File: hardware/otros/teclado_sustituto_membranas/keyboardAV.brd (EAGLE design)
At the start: 260 x 110 mm, 98 parts, among them IC1 74HC32, IC2 74LS244DW

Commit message: 
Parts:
- moved D3 63.8 mm to (10.5, 80.6), turned to 180 degrees
- moved D2 51.6 mm to (19.1, 91.8), turned to 270 degrees
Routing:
- net A9: track 0.00 -> 117.7 mm
- net A10: track 0.00 -> 96.6 mm
- net A11: track 0.00 -> 82.0 mm
- net N$49: track 0.00 -> 63.4 mm
- net A14: track 0.00 -> 48.2 mm
- net N$60: track 0.00 -> 45.6 mm
- net A13: track 0.00 -> 34.4 mm
- net A8: track 0.00 -> 31.1 mm
- net N$53: track 0.00 -> 29.9 mm
- net N$12: track 0.00 -> 25.6 mm
- net N$6: track 0.00 -> 25.5 mm
- net N$20: track 0.00 -> 25.4 mm
- net N$45: track 0.00 -> 25.3 mm
- net N$23: track 0.00 -> 25.2 mm
- net N$13: track 0.00 -> 25.1 mm
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
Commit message: 
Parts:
- moved D1 170.5 mm to (234.3, 76.2)
- moved D4 135.4 mm to (214.9, 86.4), turned to 270 degrees
- moved D5 133.6 mm to (205.4, 20.3)
- moved D32 108.8 mm to (167.0, 71.8), turned to 90 degrees
- moved D21 102.3 mm to (166.7, 38.1), turned to 270 degrees
- moved D29 81.4 mm to (187.3, 71.8), turned to 90 degrees
- moved D8 77.9 mm to (181.9, 71.8), turned to 90 degrees
- moved D16 77.8 mm to (169.5, 71.8), turned to 90 degrees
- moved D26 76.8 mm to (164.1, 71.8), turned to 90 degrees
- moved D18 75.0 mm to (179.4, 71.8), turned to 90 degrees
- moved D7 74.4 mm to (172.1, 71.8), turned to 90 degrees
- moved D10 68.8 mm to (184.8, 71.8), turned to 90 degrees
- moved IC1 65.5 mm to (146.1, 45.7), turned to 270 degrees
- moved D9 62.8 mm to (81.9, 24.1), turned to 90 degrees
- moved D6 56.0 mm to (110.2, 26.7)
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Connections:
- removed net N$52: ENTER.2, SPACE.1
- removed net N$8: A.2, CAPS.1, CAPS1.1
- new net N$91: A.2, CAPS.2, CAPS1.1, SPACE.2
- net N$19: now also V.1; no longer V.2
- net N$28: now also V.2; no longer V.1
- net N$54: now also BREAK.2
- net N$9: now also CAPS.1, ENTER.2; no longer BREAK.2, CAPS.2, SPACE.2
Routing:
- net GND: track 0.00 -> 428.3 mm
- net N$16: track 0.00 -> 316.5 mm
- net N$69: track 0.00 -> 254.8 mm
- net N$91: track 0.00 -> 229.7 mm
- net A12: track 11.8 -> 222.6 mm
- net N$60: track 45.6 -> 250.3 mm, vias 0 -> 1
- net A8: track 31.1 -> 146.1 mm, vias 0 -> 1
- net N$17: track 0.00 -> 100.3 mm, vias 0 -> 1
- net N$82: track 0.00 -> 71.5 mm, vias 0 -> 1
- net D4: track 0.00 -> 65.2 mm
- net D0: track 0.00 -> 62.9 mm
- net N$18: track 0.00 -> 60.7 mm, vias 0 -> 1
- net N$88: track 0.00 -> 58.4 mm
- net D2: track 0.00 -> 57.0 mm, vias 0 -> 1
- net D3: track 0.00 -> 49.0 mm
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
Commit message: 
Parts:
- added D34: (no value), diode:SOD323-R
- moved D11 33.0 mm to (56.2, 26.7), turned to 90 degrees
- moved D22 32.6 mm to (47.6, 17.5)
- moved D12 32.3 mm to (59.4, 27.9), turned to 90 degrees
- moved D31 15.6 mm to (69.8, 35.9)
- moved D33 14.0 mm to (77.5, 35.9)
- moved D6 13.0 mm to (97.2, 26.7)
- moved R2 3.49 mm to (93.7, 24.1)
- moved D3 2.01 mm to (20.3, 93.3)
- moved D2 0.63 mm to (8.26, 94.6)
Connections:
- removed net N$69: SPACE.4, SYMB.3, SYMB1.3
- removed net N$76: COMMA.4, PERIOD.3
- removed net N$78: COMMA.2, D11.C
- removed net N$82: D6.C, PERIOD.1, R2.2
- net A15: now also PERIOD.3, SPACE.4, SYMB.3, SYMB1.3; no longer SPACE.3
- net A8: now also D34.C
- net N$73: now also D34.A
- net N$79: now also D6.C, PERIOD.1, R2.2; no longer PERIOD.2
- net N$83: now also COMMA.2, D11.C; no longer COMMA.1
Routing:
- net A15: track 0.00 -> 428.2 mm, vias 0 -> 1
- net N$69: track 254.8 -> 0.00 mm
- net N$82: track 71.5 -> 0.00 mm, vias 1 -> 0
- net N$83: track 7.84 -> 69.4 mm, vias 0 -> 1
- net N$79: track 0.00 -> 55.1 mm, vias 0 -> 1
- net A8: track 146.1 -> 159.8 mm
- net N$4: track 0.00 -> 7.52 mm, vias 0 -> 1
- net N$70: track 72.9 -> 78.1 mm, vias 0 -> 1
- net N$60: track 250.3 -> 246.1 mm
- net N$3: track 0.00 -> 3.82 mm, vias 0 -> 1
- net VCC: track 8.25 -> 4.76 mm

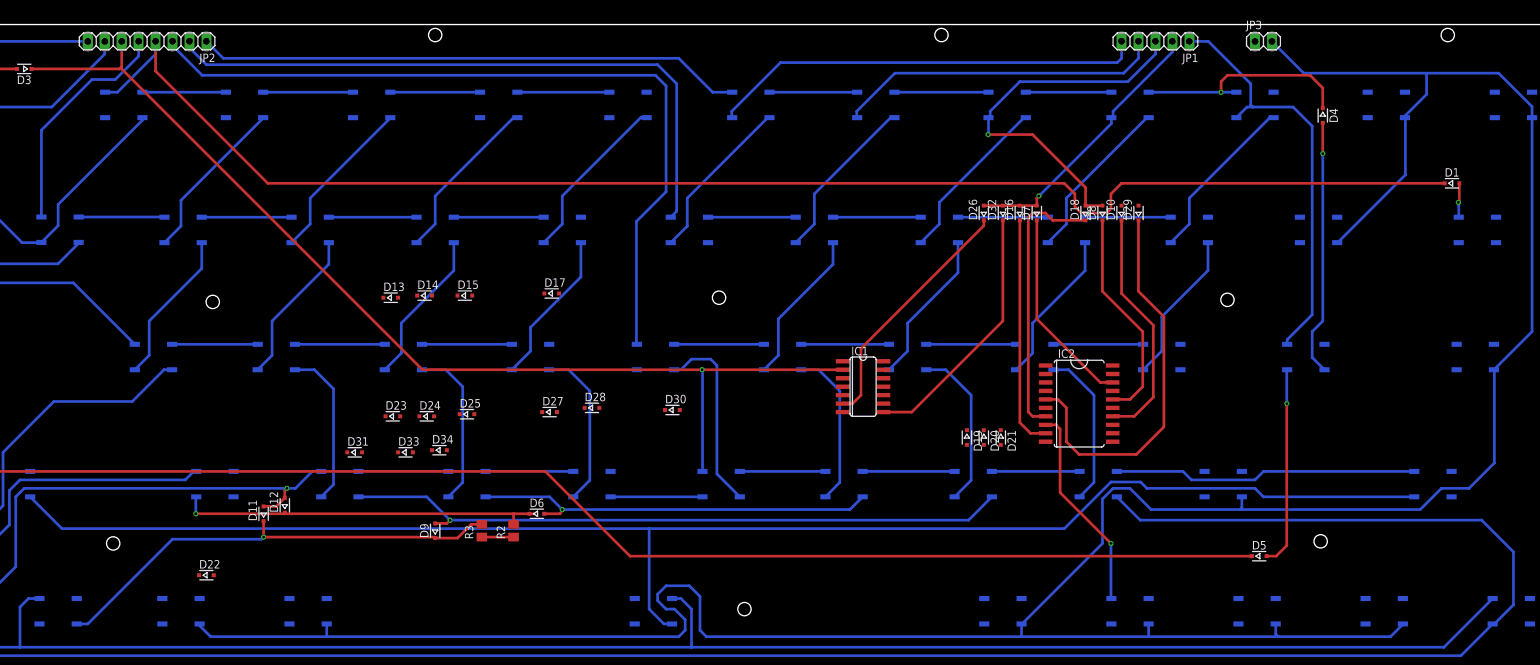
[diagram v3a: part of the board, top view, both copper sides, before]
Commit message: 
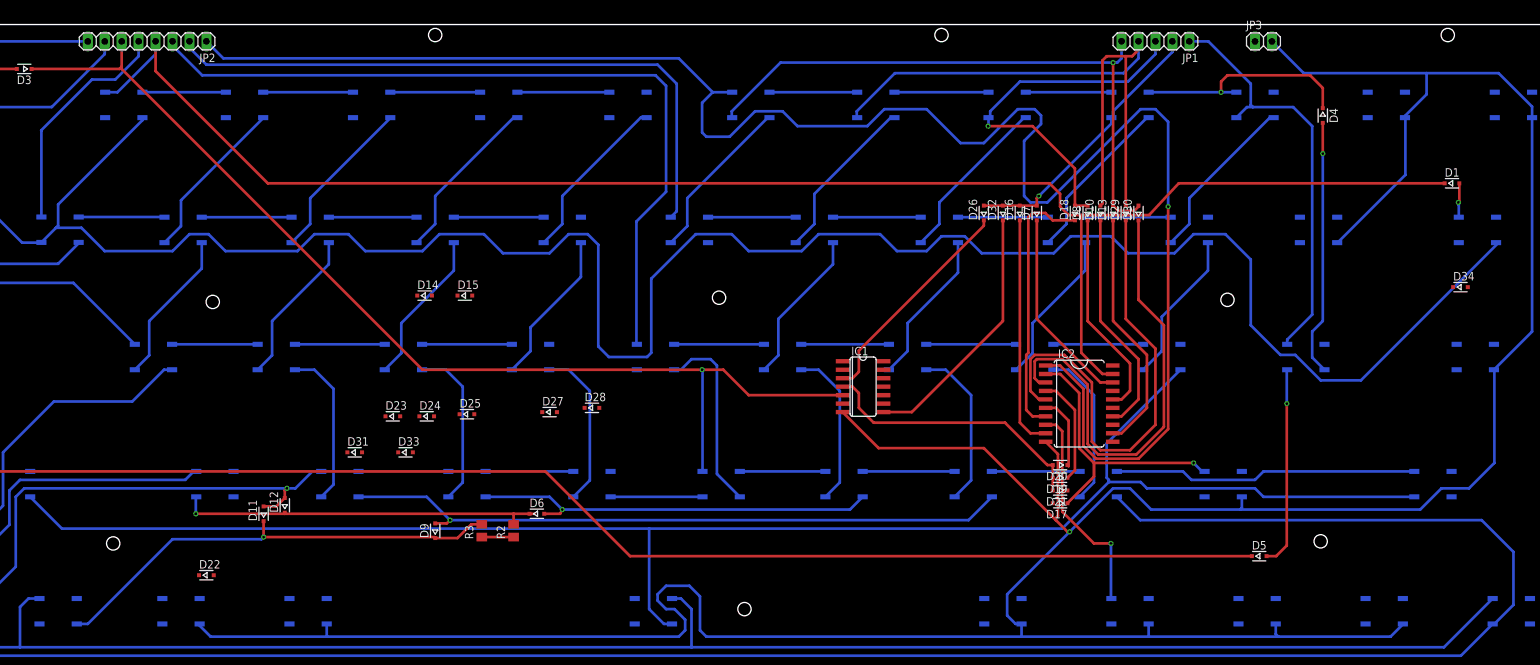
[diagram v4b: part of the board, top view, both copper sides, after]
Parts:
- moved D34 155.0 mm to (235.6, 60.6)
- moved D13 109.0 mm to (183.5, 71.8), turned to 90 degrees
- moved D17 82.4 mm to (175.6, 28.3), turned to 180 degrees
- moved D30 75.8 mm to (187.3, 71.8), turned to 90 degrees
- moved D19 15.2 mm to (175.6, 32.1), turned to 180 degrees
- moved D20 12.2 mm to (175.6, 34.0), turned to 180 degrees
- moved D21 11.9 mm to (175.6, 30.2), turned to 180 degrees
- moved D10 3.17 mm to (181.6, 71.8)
- moved D8 2.22 mm to (179.7, 71.8)
- moved D29 1.91 mm to (185.4, 71.8)
- moved D18 1.59 mm to (177.8, 71.8)
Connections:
- net A15: now also IC1.2; no longer IC1.5
- net A8: now also IC1.5; no longer IC1.2
- net N$84: now also IC1.6; no longer IC1.3
- net N$86: now also IC1.3; no longer IC1.6
- net N$87: now also IC1.1; no longer IC1.4
- net N$90: now also IC1.4; no longer IC1.1
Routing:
- net N$54: track 49.0 -> 337.2 mm
- net A11: track 82.0 -> 266.6 mm, vias 0 -> 1
- net N$89: track 0.00 -> 69.3 mm
- net GND: track 428.3 -> 484.7 mm, vias 0 -> 1
- net D3: track 49.0 -> 100.6 mm
- net CAPSLOCK: track 0.00 -> 42.4 mm, vias 0 -> 1
- net N$90: track 0.00 -> 41.5 mm
- net N$80: track 0.00 -> 36.9 mm
- net D4: track 65.2 -> 91.2 mm, vias 0 -> 1
- net A12: track 222.6 -> 248.3 mm
- net N$91: track 229.7 -> 251.2 mm
- net TRUEV: track 0.00 -> 16.2 mm
- net N$88: track 58.4 -> 71.8 mm
- net INVV: track 0.00 -> 11.3 mm
- net N$86: track 37.1 -> 33.3 mm
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
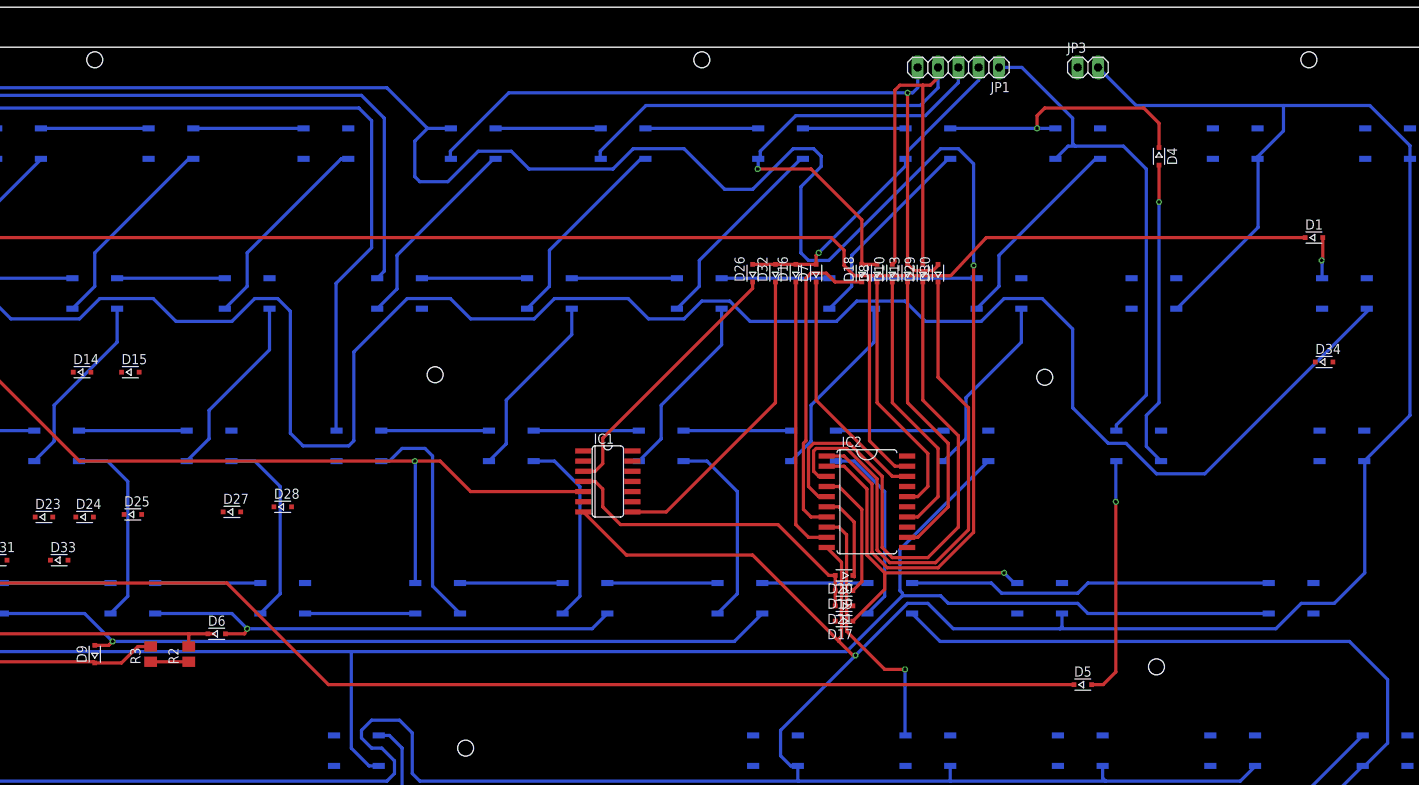
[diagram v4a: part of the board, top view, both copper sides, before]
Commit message: 
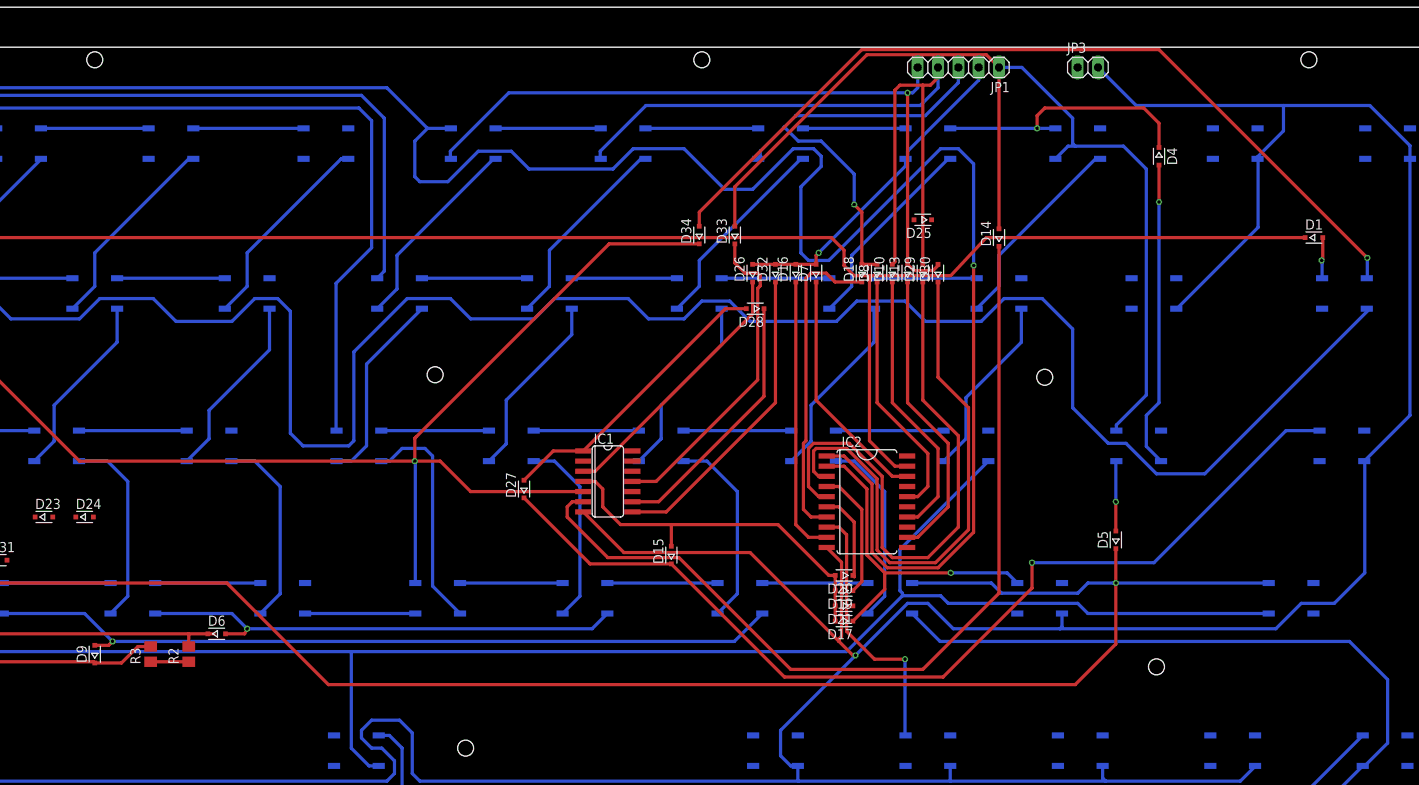
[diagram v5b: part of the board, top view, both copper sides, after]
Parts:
- moved D14 115.8 mm to (194.9, 76.2), turned to 90 degrees
- moved D25 105.4 mm to (185.4, 78.4), turned to 180 degrees
- moved D33 93.7 mm to (161.9, 76.5), turned to 90 degrees
- moved D34 79.7 mm to (157.5, 76.5), turned to 90 degrees
- moved D15 71.4 mm to (154.0, 36.5), turned to 90 degrees
- moved D28 64.0 mm to (164.5, 67.3), turned to 180 degrees
- moved D27 36.6 mm to (135.6, 44.8), turned to 90 degrees
- moved D5 18.6 mm to (209.6, 38.4), turned to 90 degrees
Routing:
- net EXTEND: track 0.00 -> 123.3 mm, vias 0 -> 1
- net N$84: track 0.00 -> 112.7 mm
- net N$73: track 0.00 -> 107.0 mm, vias 0 -> 1
- net D0: track 62.9 -> 128.5 mm
- net A8: track 161.3 -> 209.8 mm
- net N$114: track 0.00 -> 40.3 mm
- net N$87: track 0.00 -> 36.7 mm
- net SEMICOLON: track 0.00 -> 32.9 mm
- net N$27: track 0.00 -> 24.5 mm
- net N$2: track 30.1 -> 8.77 mm
- net N$60: track 246.1 -> 265.3 mm, vias 1 -> 2
- net N$90: track 41.5 -> 46.1 mm
- net LEFT: track 33.3 -> 34.0 mm

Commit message: 
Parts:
- moved D23 112.4 mm to (188.0, 44.8)
- moved D24 107.3 mm to (188.0, 41.9)
- moved D31 85.4 mm to (153.0, 55.2), turned to 90 degrees
- moved D25 39.1 mm to (188.0, 39.4), turned to 0 degrees
- moved D4 0.32 mm to (214.6, 86.4)
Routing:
- net INVV: track 11.3 -> 166.0 mm, vias 0 -> 1
- net TRUEV: track 16.2 -> 137.4 mm, vias 0 -> 1
- net GRAPHICS: track 0.00 -> 51.8 mm, vias 0 -> 3
- net RIGHT: track 0.00 -> 40.9 mm, vias 0 -> 1
- net N$90: track 46.1 -> 74.5 mm, vias 0 -> 2
- net N$91: track 251.2 -> 265.1 mm
- net QUOTES: track 0.00 -> 10.1 mm
- net N$15: track 23.8 -> 29.6 mm
- net UP: track 0.00 -> 4.32 mm
- net N$87: track 36.7 -> 39.0 mm
- net N$86: track 33.3 -> 35.4 mm
- net N$88: track 71.8 -> 72.9 mm
- net GND: track 484.7 -> 485.8 mm
- net A11: track 266.6 -> 267.2 mm
- net N$89: track 69.3 -> 69.9 mm

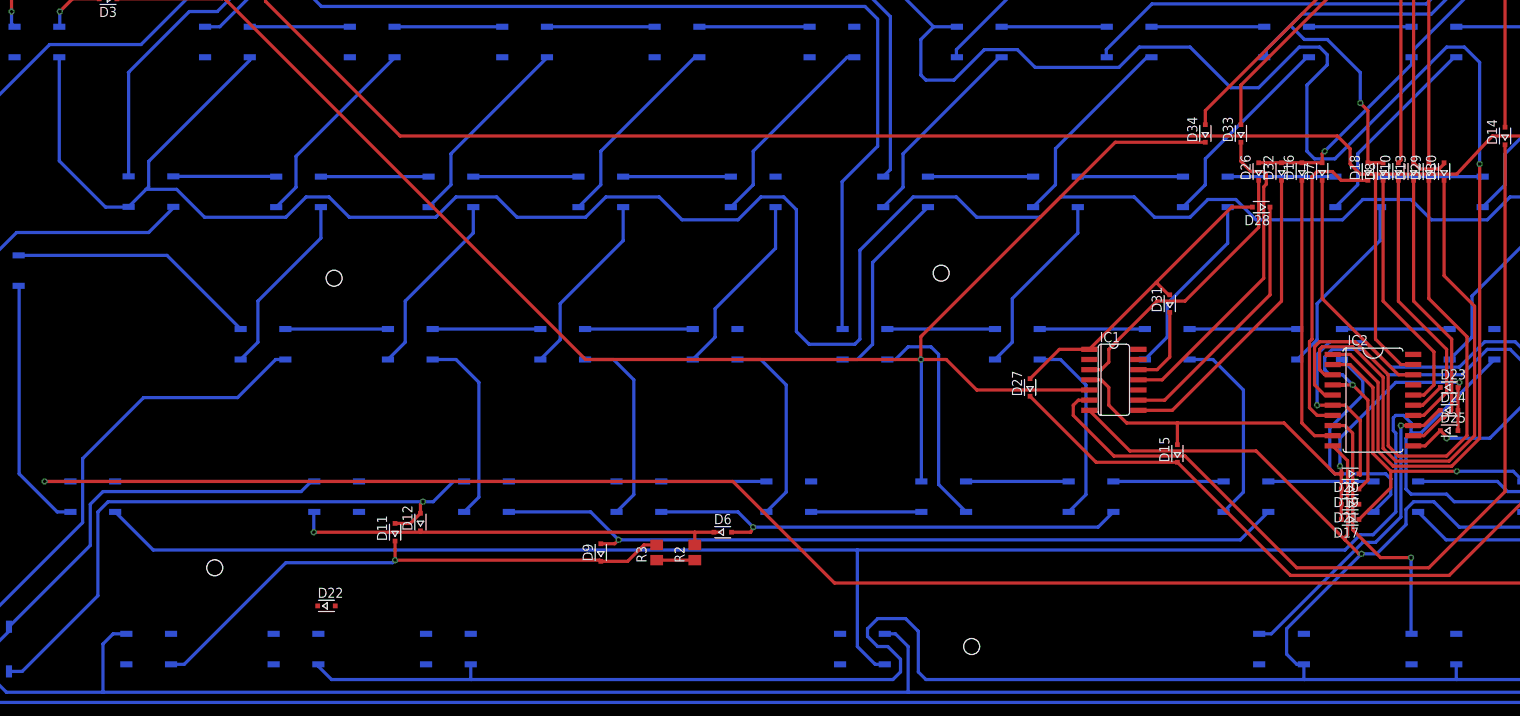
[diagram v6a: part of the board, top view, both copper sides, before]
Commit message: 
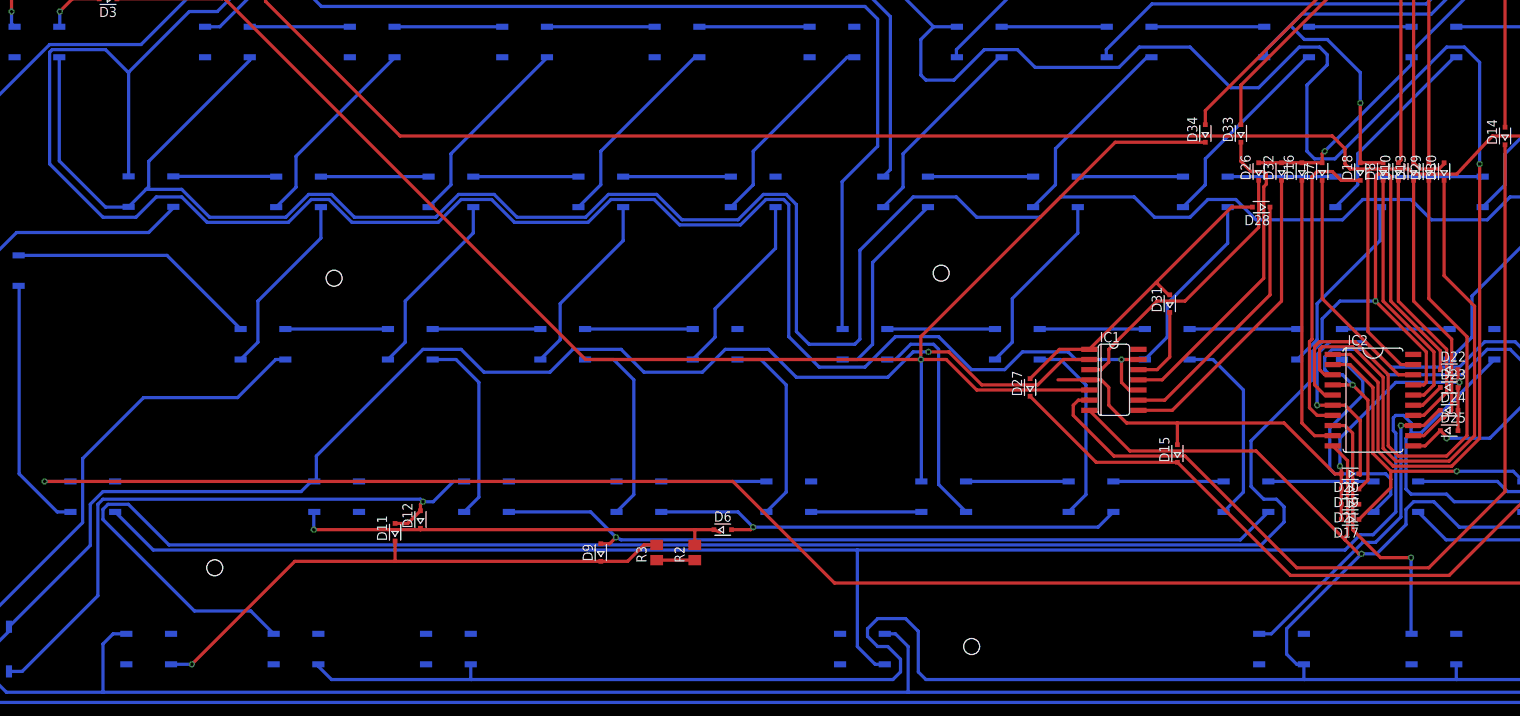
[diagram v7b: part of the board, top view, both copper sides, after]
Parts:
- moved D22 143.4 mm to (188.0, 47.0)
- moved D18 0.95 mm to (176.8, 71.8)
- moved D12 0.32 mm to (59.4, 28.3)
- moved D6 0.32 mm to (97.2, 27.0)
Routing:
- net DOWN: track 0.00 -> 278.0 mm, vias 0 -> 1
- net A13: track 34.4 -> 237.7 mm, vias 0 -> 1
- net A15: track 428.2 -> 544.1 mm, vias 1 -> 2
- net N$90: track 74.5 -> 80.1 mm
- net N$54: track 337.2 -> 338.6 mm
- net A12: track 248.3 -> 249.3 mm
- net N$85: track 40.0 -> 39.1 mm
- net N$70: track 78.1 -> 78.8 mm
- net N$28: track 28.6 -> 29.2 mm
- net D2: track 56.0 -> 56.6 mm

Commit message: Finalizado el teclado sustituto de membranas
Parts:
- moved D18 0.95 mm to (175.9, 71.8)
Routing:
- net VCC: track 4.76 -> 194.3 mm, vias 0 -> 5
- net UP: track 4.32 -> 162.2 mm, vias 0 -> 1
- net SEMICOLON: track 32.9 -> 121.9 mm, vias 0 -> 3
- net QUOTES: track 10.1 -> 80.1 mm, vias 0 -> 3
- net D0: track 128.5 -> 136.8 mm
- net N$91: track 265.1 -> 269.9 mm
- net N$90: track 80.1 -> 76.2 mm
- net N$58: track 13.8 -> 16.1 mm
- net N$15: track 29.6 -> 28.4 mm
- net N$85: track 39.1 -> 38.1 mm
- net GND: track 485.8 -> 486.6 mm
- net D2: track 56.6 -> 57.1 mm
